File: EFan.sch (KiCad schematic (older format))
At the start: 36 parts, among them J1 Conn_01x04_Male, J2 Conn_01x03_Male, M1 Fan, Q1 TIP41, SW1 SW_Push, U1 STM32F030F4Px, U2 LM358

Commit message: update
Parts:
- removed U?: AMS1117-3.3, Package_TO_SOT_SMD:SOT-223-3_TabPin2, symbol Regulator_Linear:AMS1117-3.3
- C9: renamed from C?; value C -> 104; footprint (none) -> Capacitor_SMD:C_0603_1608Metric_Pad1.05x0.95mm_HandSolder
- R11: renamed from R?; value R -> 126k; footprint (none) -> Resistor_SMD:R_0603_1608Metric_Pad1.05x0.95mm_HandSolder
- R12: renamed from R?; value R -> 143; footprint (none) -> Resistor_SMD:R_0603_1608Metric_Pad1.05x0.95mm_HandSolder
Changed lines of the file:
@@
 $EndComp
 $Comp
-L Device:R R?
+L Device:R R11
 U 1 1 5DBAD5E7
 P 8050 3250
-F 0 "R?" H 8120 3296 50  0000 L CNN
-F 1 "R" H 8120 3205 50  0000 L CNN
-F 2 "" V 7980 3250 50  0001 C CNN
+F 0 "R11" H 8120 3296 50  0000 L CNN
+F 1 "126k" H 8120 3205 50  0000 L CNN
+F 2 "Resistor_SMD:R_0603_1608Metric_Pad1.05x0.95mm_HandSolder" V 7980 3250 50  0001 C CNN
 F 3 "~" H 8050 3250 50  0001 C CNN
 	1    8050 3250
@@
 $EndComp
 $Comp
-L Device:R R?
+L Device:R R12
 U 1 1 5DBADFAF
 P 8050 3650
-F 0 "R?" H 8120 3696 50  0000 L CNN
-F 1 "R" H 8120 3605 50  0000 L CNN
-F 2 "" V 7980 3650 50  0001 C CNN
+F 0 "R12" H 8120 3696 50  0000 L CNN
+F 1 "143" H 8120 3605 50  0000 L CNN
+F 2 "Resistor_SMD:R_0603_1608Metric_Pad1.05x0.95mm_HandSolder" V 7980 3650 50  0001 C CNN
 F 3 "~" H 8050 3650 50  0001 C CNN
 	1    8050 3650
@@
 	7400 3050 7400 3000
 $Comp
-L Device:C C?
+L Device:C C9
 U 1 1 5DBBCF3E
 P 8450 3650
-F 0 "C?" H 8565 3696 50  0000 L CNN
-F 1 "C" H 8565 3605 50  0000 L CNN
-F 2 "" H 8488 3500 50  0001 C CNN
+F 0 "C9" H 8565 3696 50  0000 L CNN
+F 1 "104" H 8565 3605 50  0000 L CNN
+F 2 "Capacitor_SMD:C_0603_1608Metric_Pad1.05x0.95mm_HandSolder" H 8488 3500 50  0001 C CNN
 F 3 "~" H 8450 3650 50  0001 C CNN
 	1    8450 3650
@@
 Wire Wire Line
 	7750 3450 8050 3450
-$Comp
-L Regulator_Linear:AMS1117-3.3 U?
-U 1 1 5DBDFF89
-P 2250 6350
-F 0 "U?" H 2250 6592 50  0000 C CNN
-F 1 "AMS1117-3.3" H 2250 6501 50  0000 C CNN
-F 2 "Package_TO_SOT_SMD:SOT-223-3_TabPin2" H 2250 6550 50  0001 C CNN
-F 3 "http://www.advanced-monolithic.com/pdf/ds1117.pdf" H 2350 6100 50  0001 C CNN
-	1    2250 6350
-	1    0    0    -1
-$EndComp
 $EndSCHEMATC

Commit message: production 2
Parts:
- added TP1: NTC, TestPoint:TestPoint_Loop_D2.50mm_Drill1.0mm, symbol Connector:TestPoint
- added TP2: TSET, TestPoint:TestPoint_Loop_D2.50mm_Drill1.0mm, symbol Connector:TestPoint
- added TP4: DAC, TestPoint:TestPoint_Loop_D2.50mm_Drill1.0mm, symbol Connector:TestPoint
- added TP6: FB, TestPoint:TestPoint_Loop_D2.50mm_Drill1.0mm, symbol Connector:TestPoint
- TP3: renamed from TP1; value TestPoint -> GND
- TP5: renamed from TP2; value TestPoint -> 28V
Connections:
- net GND: no longer U2.5 (+)
- net at C9.1, R11.2, R12.1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: now also TP6.1
- net at R7.2, TH1.1, U1.6 (PA0): now also TP1.1
- net at R9.2, RV1.1, U1.7 (PA1): now also TP2.1
- net DAC: now reaches R17.2, U2.1, U2.2 (-)
- net DAC: now also U2.5 (+), TP4.1
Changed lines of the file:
@@
 	4550 2200 4550 2350
 Wire Wire Line
-	3700 2350 4550 2350
+	3700 2350 4200 2350
 Connection ~ 4550 2350
 Wire Wire Line
@@
 	6050 6850 5950 6850
 Wire Wire Line
-	5350 6750 5250 6750
-$Comp
-L power:GND #PWR0119
-U 1 1 5DC104D2
-P 5250 7250
-F 0 "#PWR0119" H 5250 7000 50  0001 C CNN
-F 1 "GND" H 5255 7077 50  0000 C CNN
-F 2 "" H 5250 7250 50  0001 C CNN
-F 3 "" H 5250 7250 50  0001 C CNN
-	1    5250 7250
-	1    0    0    -1
-$EndComp
-Wire Wire Line
-	5250 6750 5250 7250
-Wire Wire Line
 	5350 6950 5300 6950
 Wire Wire Line
@@
 	4300 4900 4500 4900
 $Comp
-L Connector:TestPoint TP2
+L Connector:TestPoint TP5
 U 1 1 5DB9298C
 P 7400 1900
-F 0 "TP2" V 7595 1972 50  0000 C CNN
-F 1 "TestPoint" V 7504 1972 50  0000 C CNN
+F 0 "TP5" V 7595 1972 50  0000 C CNN
+F 1 "28V" V 7504 1972 50  0000 C CNN
 F 2 "Connector_PinHeader_2.54mm:PinHeader_1x01_P2.54mm_Vertical" H 7600 1900 50  0001 C CNN
 F 3 "~" H 7600 1900 50  0001 C CNN
@@
 $EndComp
 $Comp
-L Connector:TestPoint TP1
+L Connector:TestPoint TP3
 U 1 1 5DB93746
 P 6500 7450
-F 0 "TP1" V 6695 7522 50  0000 C CNN
-F 1 "TestPoint" V 6604 7522 50  0000 C CNN
+F 0 "TP3" V 6695 7522 50  0000 C CNN
+F 1 "GND" V 6604 7522 50  0000 C CNN
 F 2 "Connector_PinHeader_2.54mm:PinHeader_1x01_P2.54mm_Vertical" H 6700 7450 50  0001 C CNN
 F 3 "~" H 6700 7450 50  0001 C CNN
@@
 Wire Wire Line
 	7750 3450 8050 3450
+Text Label 5100 6750 0    50   ~ 0
+DAC
+Wire Wire Line
+	5100 6750 5350 6750
+Wire Wire Line
+	6600 3750 7050 3750
+Connection ~ 6600 3750
+Text Label 7050 3750 2    50   ~ 0
+DAC
+$Comp
+L Connector:TestPoint TP4
+U 1 1 5DC70BC2
+P 6600 3350
+F 0 "TP4" H 6658 3468 50  0000 L CNN
+F 1 "DAC" H 6658 3377 50  0000 L CNN
+F 2 "TestPoint:TestPoint_Loop_D2.50mm_Drill1.0mm" H 6800 3350 50  0001 C CNN
+F 3 "~" H 6800 3350 50  0001 C CNN
+	1    6600 3350
+	1    0    0    -1
+$EndComp
+Connection ~ 6600 3350
+$Comp
+L Connector:TestPoint TP1
+U 1 1 5DC71FEC
+P 4200 2350
+F 0 "TP1" H 4258 2468 50  0000 L CNN
+F 1 "NTC" H 4258 2377 50  0000 L CNN
+F 2 "TestPoint:TestPoint_Loop_D2.50mm_Drill1.0mm" H 4400 2350 50  0001 C CNN
+F 3 "~" H 4400 2350 50  0001 C CNN
+	1    4200 2350
+	1    0    0    -1
+$EndComp
+Connection ~ 4200 2350
+Wire Wire Line
+	4200 2350 4550 2350
+$Comp
+L Connector:TestPoint TP2
+U 1 1 5DC7279B
+P 5200 2450
+F 0 "TP2" V 5154 2638 50  0000 L CNN
+F 1 "TSET" V 5245 2638 50  0000 L CNN
+F 2 "TestPoint:TestPoint_Loop_D2.50mm_Drill1.0mm" H 5400 2450 50  0001 C CNN
+F 3 "~" H 5400 2450 50  0001 C CNN
+	1    5200 2450
+	0    1    1    0
+$EndComp
+$Comp
+L Connector:TestPoint TP6
+U 1 1 5DC732A9
+P 7750 3450
+F 0 "TP6" H 7808 3568 50  0000 L CNN
+F 1 "FB" H 7808 3477 50  0000 L CNN
+F 2 "TestPoint:TestPoint_Loop_D2.50mm_Drill1.0mm" H 7950 3450 50  0001 C CNN
+F 3 "~" H 7950 3450 50  0001 C CNN
+	1    7750 3450
+	1    0    0    -1
+$EndComp
+Connection ~ 7750 3450
 $EndSCHEMATC

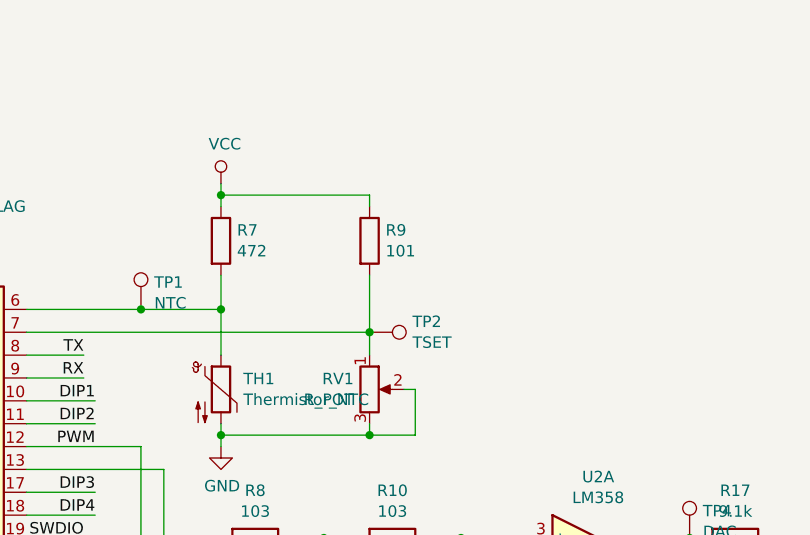
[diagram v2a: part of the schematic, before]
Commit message: incr r9, to limit current usage
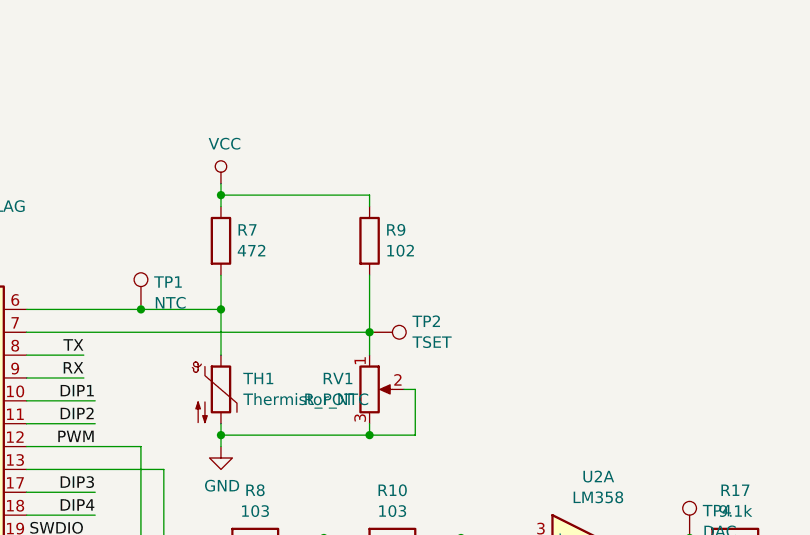
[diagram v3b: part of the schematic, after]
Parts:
- R9: value 101 -> 102
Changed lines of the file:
@@
 P 5200 2050
 F 0 "R9" H 5270 2096 50  0000 L CNN
-F 1 "101" H 5270 2005 50  0000 L CNN
+F 1 "102" H 5270 2005 50  0000 L CNN
 F 2 "Resistor_SMD:R_0603_1608Metric_Pad1.05x0.95mm_HandSolder" V 5130 2050 50  0001 C CNN
 F 3 "~" H 5200 2050 50  0001 C CNN

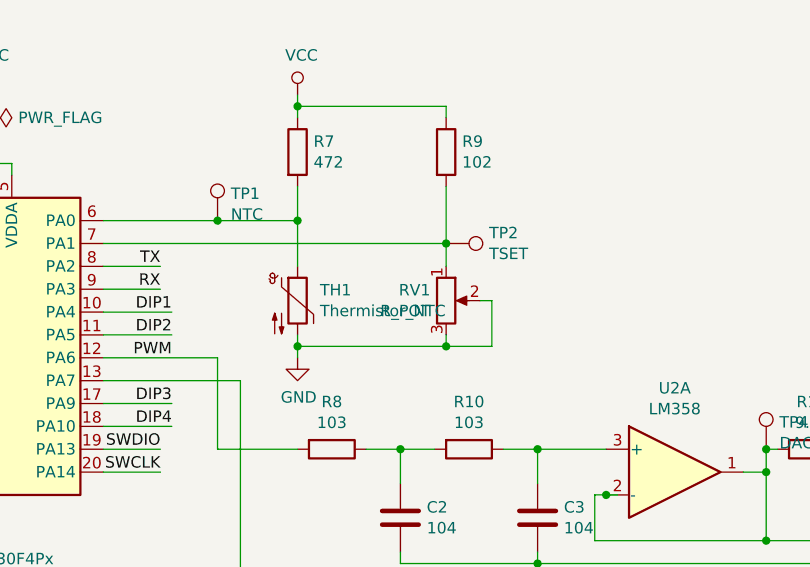
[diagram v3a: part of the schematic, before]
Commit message: add 2 coupling caps in adc input
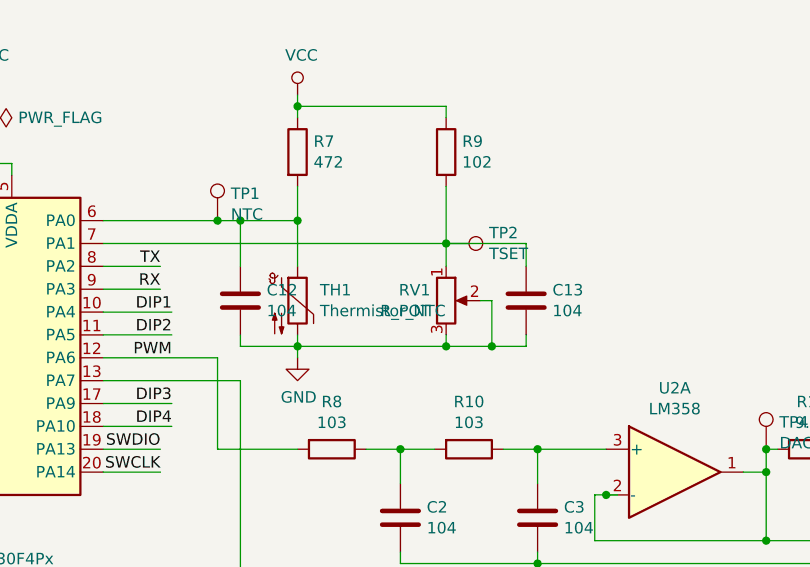
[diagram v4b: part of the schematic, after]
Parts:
- added C12, C13: 104, Capacitor_SMD:C_0603_1608Metric_Pad1.05x0.95mm_HandSolder, symbol Device:C
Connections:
- net GND: now also C12.2, C13.2
- net at R7.2, TH1.1, TP1.1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: now also C12.1
- net at R9.2, RV1.1, TP2.1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: now also C13.1
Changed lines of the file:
@@
 Connection ~ 4200 2350
 Wire Wire Line
-	4200 2350 4550 2350
+	4200 2350 4300 2350
 $Comp
 L Connector:TestPoint TP2
@@
 $EndComp
 Connection ~ 7750 3450
+$Comp
+L Device:C C13
+U 1 1 5DC6CB68
+P 5550 2700
+F 0 "C13" H 5665 2746 50  0000 L CNN
+F 1 "104" H 5665 2655 50  0000 L CNN
+F 2 "Capacitor_SMD:C_0603_1608Metric_Pad1.05x0.95mm_HandSolder" H 5588 2550 50  0001 C CNN
+F 3 "~" H 5550 2700 50  0001 C CNN
+	1    5550 2700
+	1    0    0    -1
+$EndComp
+$Comp
+L Device:C C12
+U 1 1 5DC6D19A
+P 4300 2700
+F 0 "C12" H 4415 2746 50  0000 L CNN
+F 1 "104" H 4415 2655 50  0000 L CNN
+F 2 "Capacitor_SMD:C_0603_1608Metric_Pad1.05x0.95mm_HandSolder" H 4338 2550 50  0001 C CNN
+F 3 "~" H 4300 2700 50  0001 C CNN
+	1    4300 2700
+	1    0    0    -1
+$EndComp
+Wire Wire Line
+	4300 2850 4300 2900
+Wire Wire Line
+	4300 2900 4550 2900
+Wire Wire Line
+	4300 2550 4300 2350
+Connection ~ 4300 2350
+Wire Wire Line
+	4300 2350 4550 2350
+Wire Wire Line
+	5550 2550 5550 2450
+Wire Wire Line
+	5550 2450 5200 2450
+Wire Wire Line
+	5550 2850 5550 2900
+Wire Wire Line
+	5550 2900 5400 2900
+Connection ~ 5400 2900
 $EndSCHEMATC
